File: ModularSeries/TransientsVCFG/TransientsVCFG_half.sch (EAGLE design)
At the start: 88 parts, among them IC2 4013N, Q1 2N3906, Q2 2N3906, Q3 2N3906, Q4 2N3906, Q5 2N3904, Q6 2N3904

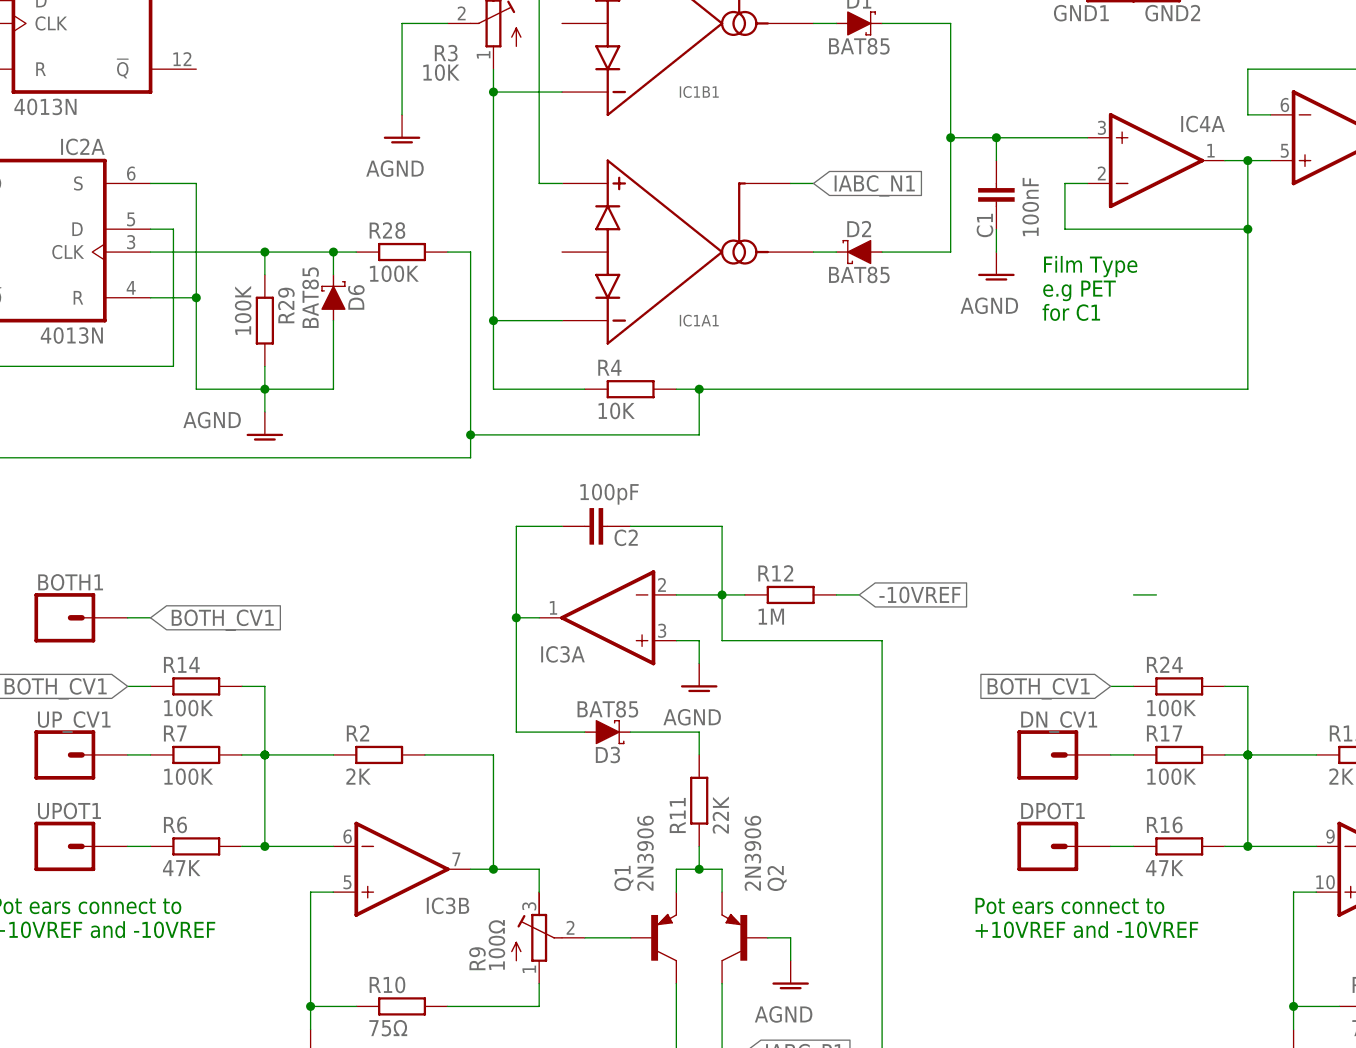
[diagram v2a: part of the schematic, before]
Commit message: Saltwaters BOM added
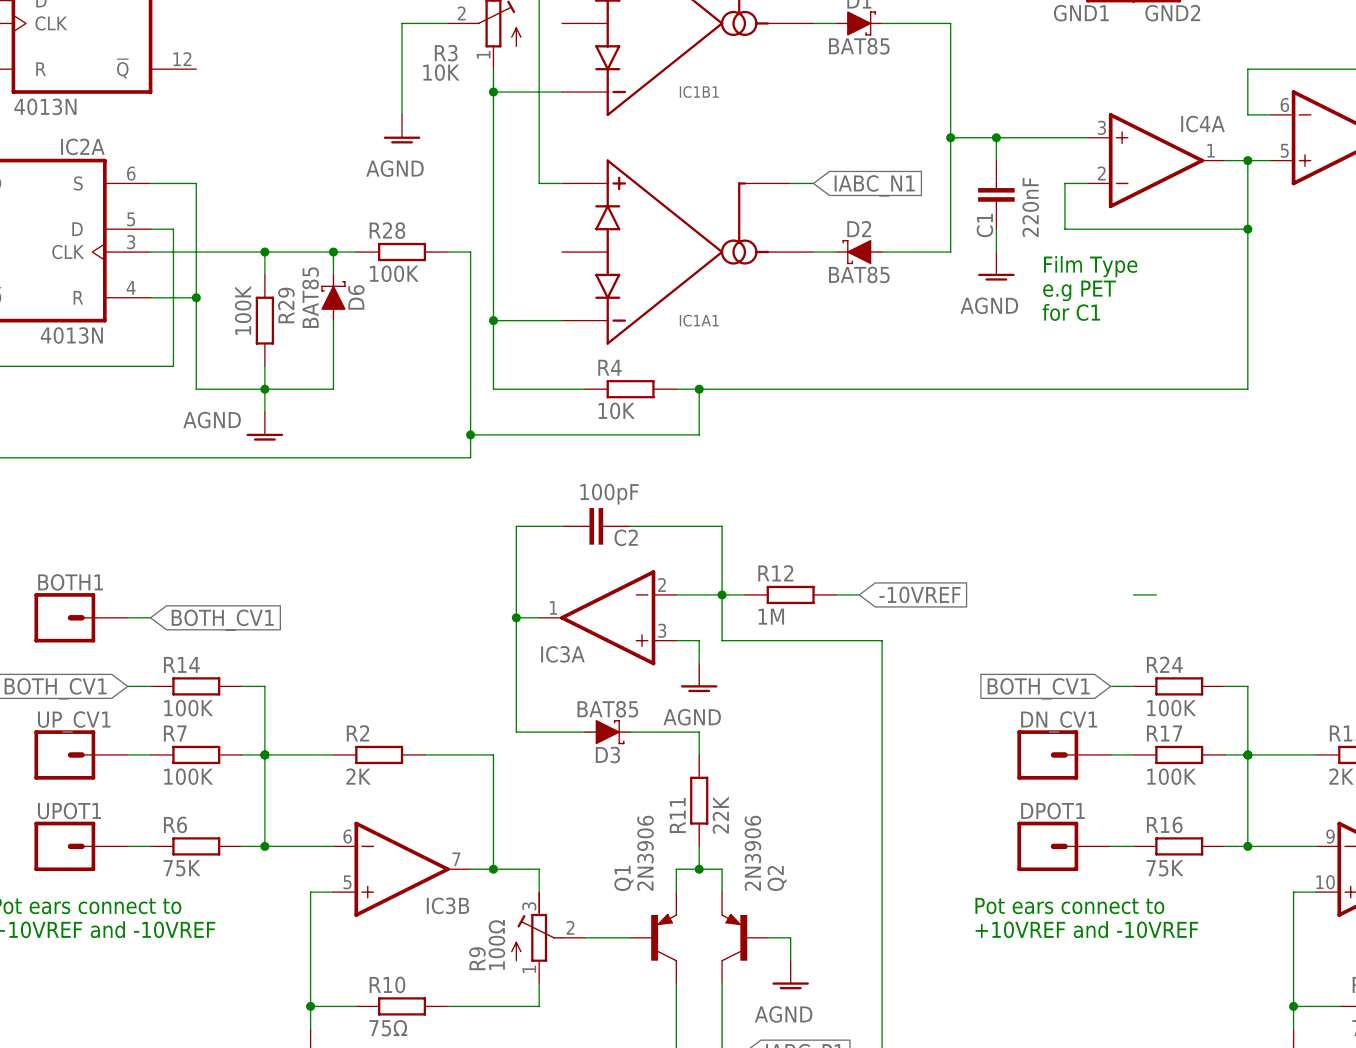
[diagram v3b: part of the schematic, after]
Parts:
- C1: value 100nF -> 220nF
- R16, R6: value 47K -> 75K
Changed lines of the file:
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@@
 <part name="R2" library="rcl" library_urn="urn:adsk.eagle:library:334" deviceset="R-EU_" device="0207/10" package3d_urn="urn:adsk.eagle:package:23491/2" value="2K"/>
 <part name="R3" library="rcl" library_urn="urn:adsk.eagle:library:334" deviceset="R-TRIMM" device="3296W" package3d_urn="urn:adsk.eagle:package:26033/1" value="10K"/>
-<part name="C1" library="rcl" library_urn="urn:adsk.eagle:library:334" deviceset="C-EU" device="050-025X075" package3d_urn="urn:adsk.eagle:package:23637/1" value="100nF"/>
+<part name="C1" library="rcl" library_urn="urn:adsk.eagle:library:334" deviceset="C-EU" device="050-025X075" package3d_urn="urn:adsk.eagle:package:23637/1" value="220nF"/>
 <part name="AGND1" library="supply1" library_urn="urn:adsk.eagle:library:371" deviceset="AGND" device=""/>
 <part name="R4" library="rcl" library_urn="urn:adsk.eagle:library:334" deviceset="R-EU_" device="0207/10" package3d_urn="urn:adsk.eagle:package:23491/2" value="10K"/>
@@
 <part name="IC4" library="ElectricNoodleBox" deviceset="TL0X2" device="DIL" package3d_urn="urn:adsk.eagle:package:29519/2"/>
 <part name="AGND3" library="supply1" library_urn="urn:adsk.eagle:library:371" deviceset="AGND" device=""/>
-<part name="R6" library="rcl" library_urn="urn:adsk.eagle:library:334" deviceset="R-EU_" device="0207/10" package3d_urn="urn:adsk.eagle:package:23491/2" value="47K"/>
+<part name="R6" library="rcl" library_urn="urn:adsk.eagle:library:334" deviceset="R-EU_" device="0207/10" package3d_urn="urn:adsk.eagle:package:23491/2" value="75K"/>
 <part name="R7" library="rcl" library_urn="urn:adsk.eagle:library:334" deviceset="R-EU_" device="0207/10" package3d_urn="urn:adsk.eagle:package:23491/2" value="100K"/>
 <part name="Q1" library="transistor-pnp" library_urn="urn:adsk.eagle:library:399" deviceset="2N3906" device="" package3d_urn="urn:adsk.eagle:package:29211/2"/>
@@
 <part name="R15" library="rcl" library_urn="urn:adsk.eagle:library:334" deviceset="R-EU_" device="0207/10" package3d_urn="urn:adsk.eagle:package:23491/2" value="2K"/>
 <part name="AGND6" library="supply1" library_urn="urn:adsk.eagle:library:371" deviceset="AGND" device=""/>
-<part name="R16" library="rcl" library_urn="urn:adsk.eagle:library:334" deviceset="R-EU_" device="0207/10" package3d_urn="urn:adsk.eagle:package:23491/2" value="47K"/>
+<part name="R16" library="rcl" library_urn="urn:adsk.eagle:library:334" deviceset="R-EU_" device="0207/10" package3d_urn="urn:adsk.eagle:package:23491/2" value="75K"/>
 <part name="R17" library="rcl" library_urn="urn:adsk.eagle:library:334" deviceset="R-EU_" device="0207/10" package3d_urn="urn:adsk.eagle:package:23491/2" value="100K"/>
 <part name="Q3" library="transistor-pnp" library_urn="urn:adsk.eagle:library:399" deviceset="2N3906" device="" package3d_urn="urn:adsk.eagle:package:29211/2"/>
